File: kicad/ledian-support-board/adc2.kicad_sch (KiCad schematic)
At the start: 17 parts, among them U7 MCP3208, U9 REF3030

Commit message: kicad: ledian-support-board: added titles to all pages
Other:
- title: (none) -> ADC2
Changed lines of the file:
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@@
 (kicad_sch (version 20230121) (generator eeschema)
   (paper "A4")
+  (title_block
+    (title "ADC2")
+  )
   (junction (at 156.21 78.74) (diameter 0) (color 0 0 0 0)
   )

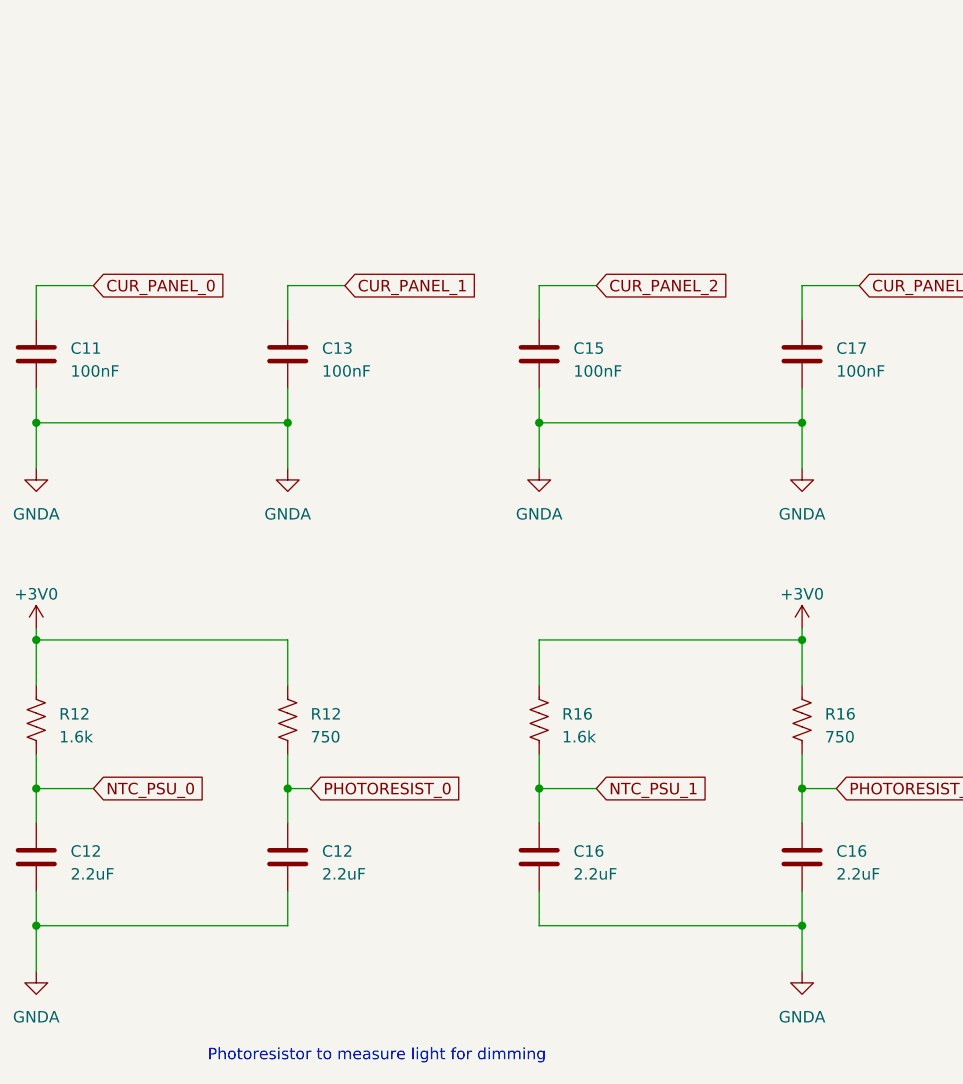
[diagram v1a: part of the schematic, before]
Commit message: kicad: ledian-support-board: added some comments to parts of the circuit
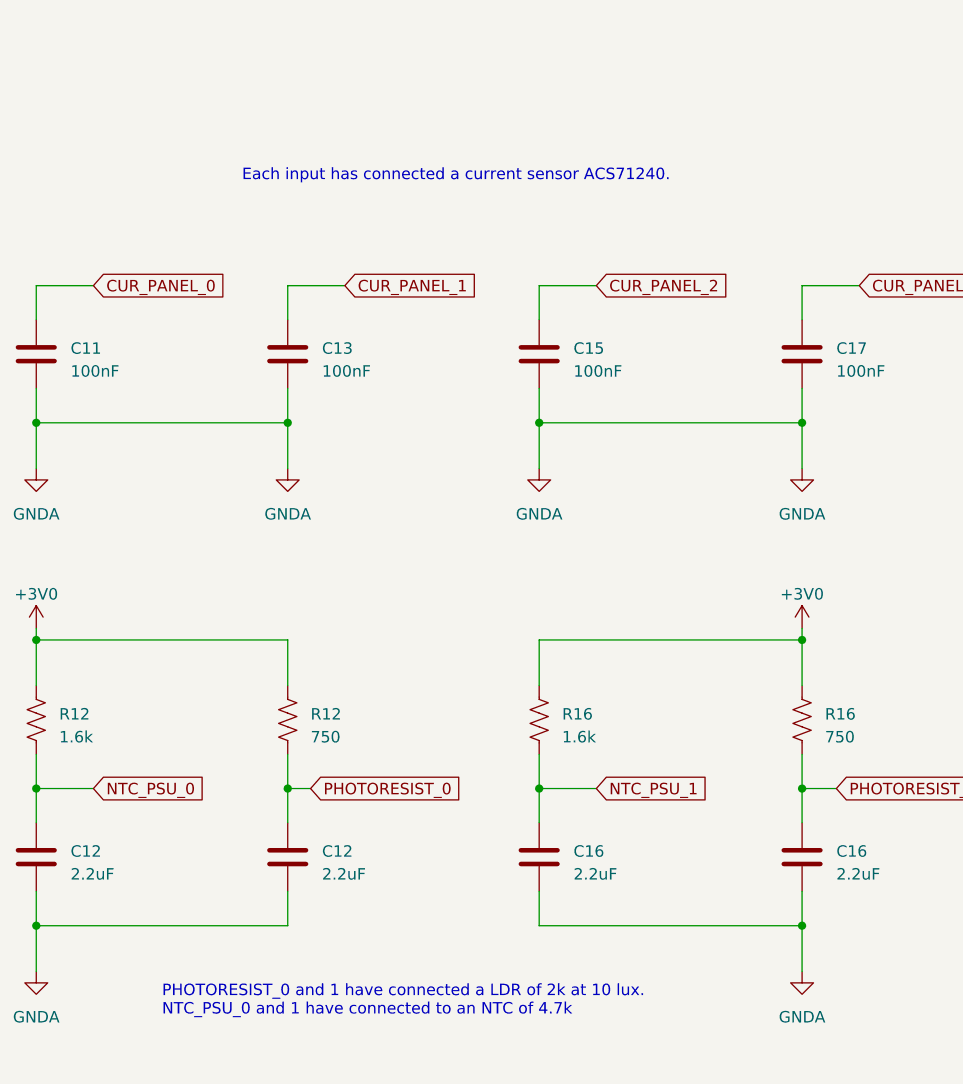
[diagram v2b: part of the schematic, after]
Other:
- note added: "Each input has connected a current sensor ACS71240."
- note added: "PHOTORESIST_0 and 1 have connected a LDR of 2k at 10 lux. NTC_PSU_0 and 1 have connected to an NTC of 4.7k"
- note removed: "Photoresistor to measure light for dimming"
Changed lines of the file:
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@@
     (stroke (width 0) (type default))
   )
-  (text "Photoresistor to measure light for dimming" (at 175.26 149.86 0)
+  (text "Each input has connected a current sensor ACS71240."
+    (at 179.07 52.07 0)
     (effects (font (size 1.27 1.27)) (justify left bottom))
   )
+  (text "PHOTORESIST_0 and 1 have connected a LDR of 2k at 10 lux.\nNTC_PSU_0 and 1 have connected to an NTC of 4.7k"
+    (at 170.18 144.78 0)
+    (effects (font (size 1.27 1.27)) (justify left bottom))
+  )
